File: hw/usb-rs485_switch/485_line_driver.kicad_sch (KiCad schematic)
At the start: 26 parts, among them Q1 MMBT5551, Q2 Si2301CDS, U12 INA180A1, U13 MAX485E

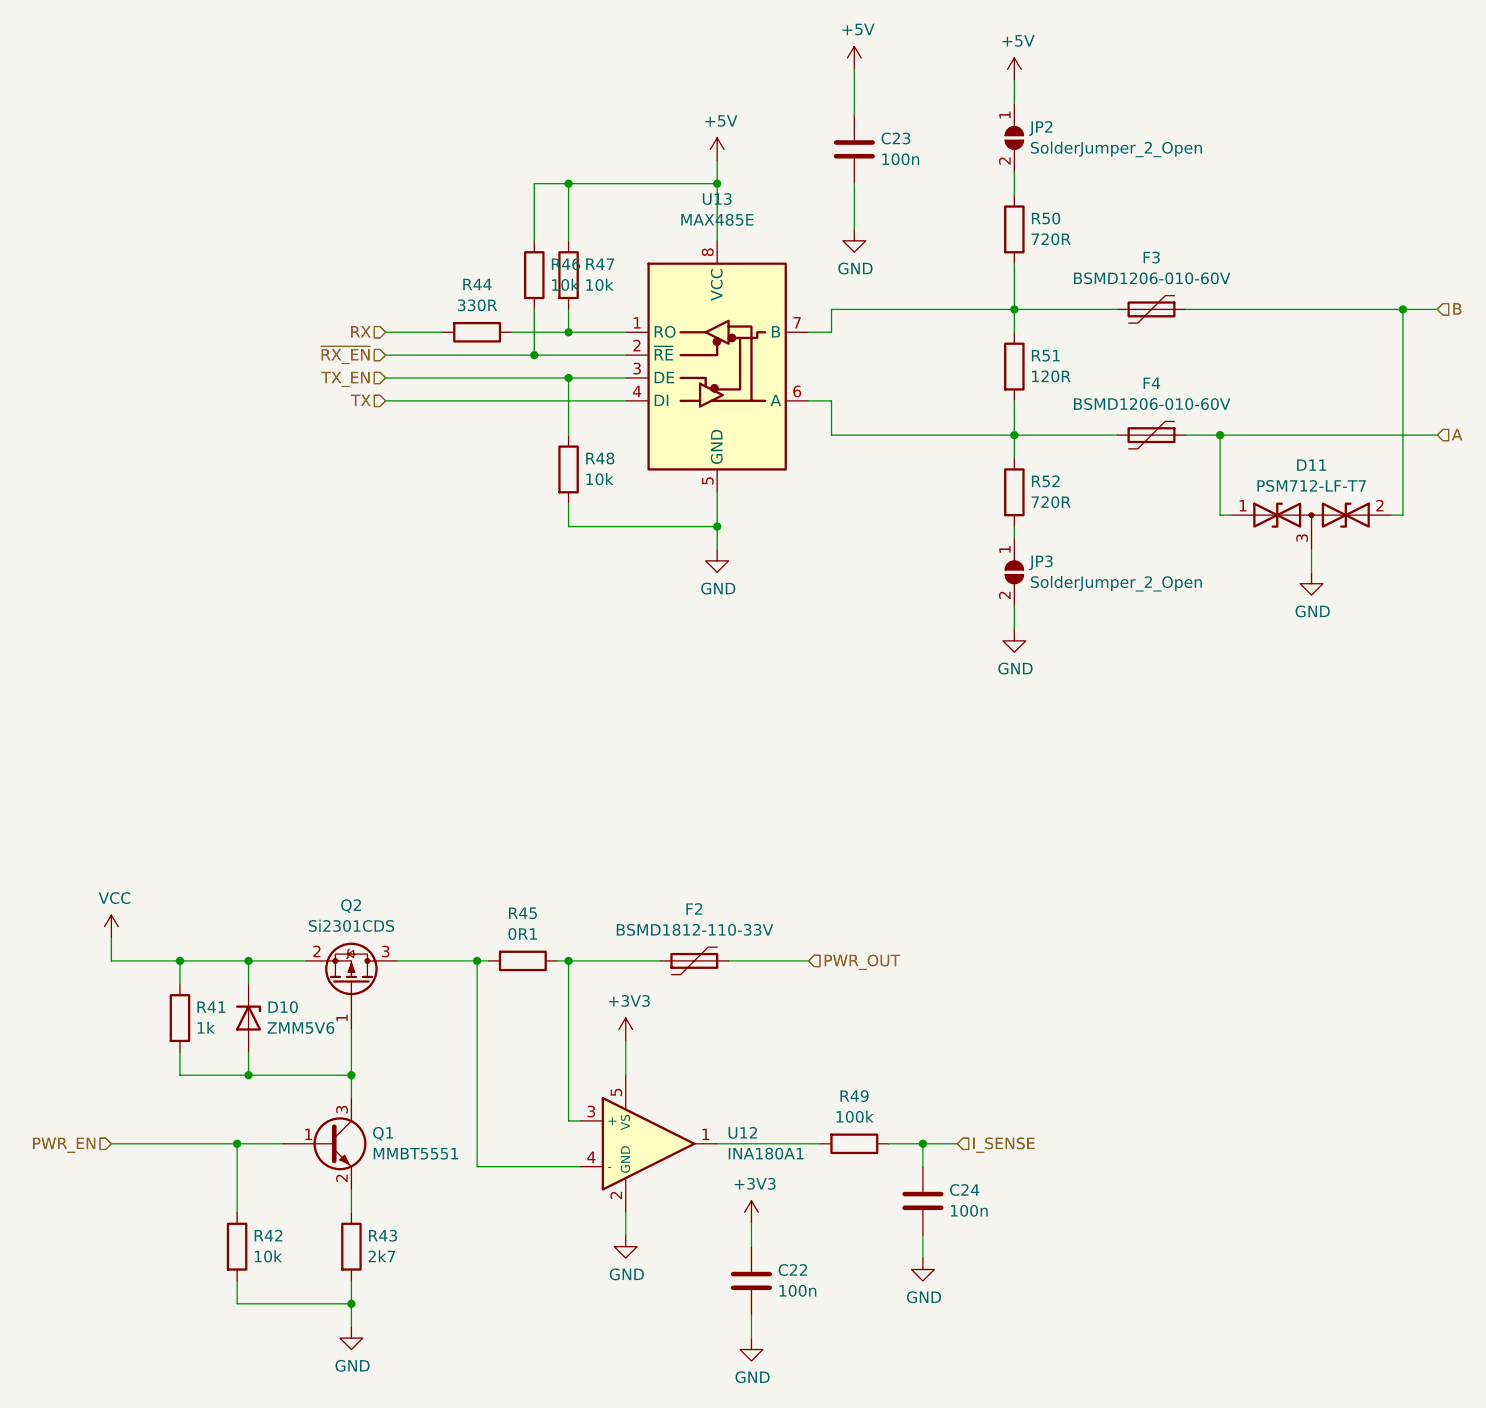
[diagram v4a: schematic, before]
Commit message: Removed unused DCDC, board labels.
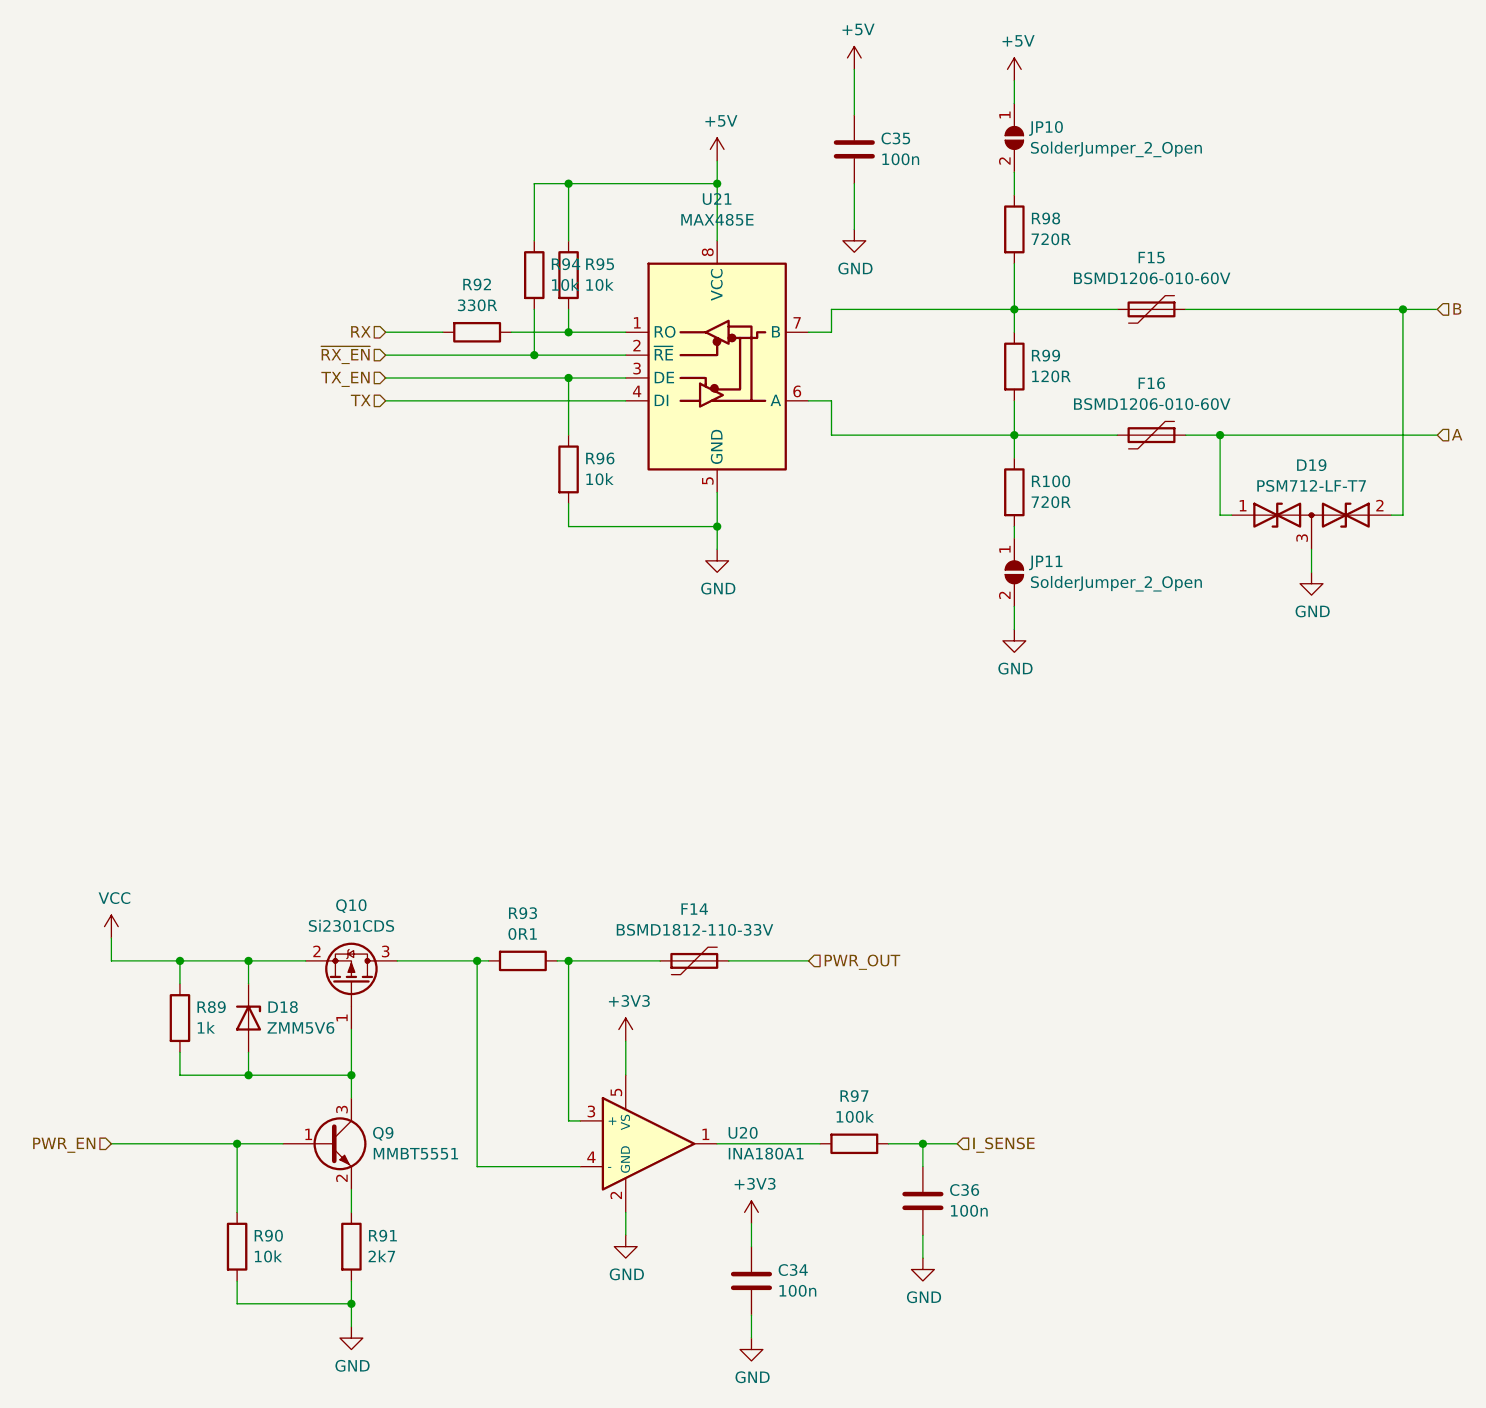
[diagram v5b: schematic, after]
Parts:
- renumbered C22 to C34, C23 to C35, C24 to C36, D10 to D18, D11 to D19, F2 to F14, F3 to F15, F4 to F16, JP2 to JP10, JP3 to JP11, Q2 to Q10, Q1 to Q9, R52 to R100, R41 to R89, R42 to R90, R43 to R91, R44 to R92, R45 to R93, R46 to R94, R47 to R95, R48 to R96, R49 to R97, R50 to R98, R51 to R99, U12 to U20, U13 to U21
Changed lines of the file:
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@@
   (symbol (lib_id "Interface_UART:MAX485E") (at 118.11 67.31 0)
     (in_bom yes) (on_board yes)
-    (property "Reference" "U13" (id 0) (at 118.11 50.0126 0))
+    (property "Reference" "U21" (id 0) (at 118.11 50.0126 0))
     (property "Value" "MAX485E" (id 1) (at 118.11 52.324 0))
     (property "Footprint" "Package_SO:SOIC-8_3.9x4.9mm_P1.27mm" (id 2) (at 118.11 85.09 0)
@@
   (symbol (lib_id "Device:R") (at 151.13 53.34 0)
     (in_bom yes) (on_board yes)
-    (property "Reference" "R50" (id 0) (at 152.908 52.1716 0)
+    (property "Reference" "R98" (id 0) (at 152.908 52.1716 0)
       (effects (font (size 1.27 1.27)) (justify left))
     )
@@
   (symbol (lib_id "Device:R") (at 151.13 68.58 0)
     (in_bom yes) (on_board yes)
-    (property "Reference" "R51" (id 0) (at 152.908 67.4116 0)
+    (property "Reference" "R99" (id 0) (at 152.908 67.4116 0)
       (effects (font (size 1.27 1.27)) (justify left))
     )
@@
   (symbol (lib_id "Device:R") (at 151.13 82.55 0)
     (in_bom yes) (on_board yes)
-    (property "Reference" "R52" (id 0) (at 152.908 81.3816 0)
+    (property "Reference" "R100" (id 0) (at 152.908 81.3816 0)
       (effects (font (size 1.27 1.27)) (justify left))
     )
@@
   (symbol (lib_id "Device:Polyfuse") (at 166.37 62.23 270)
     (in_bom yes) (on_board yes)
-    (property "Reference" "F3" (id 0) (at 166.37 56.515 90))
+    (property "Reference" "F15" (id 0) (at 166.37 56.515 90))
     (property "Value" "BSMD1206-010-60V" (id 1) (at 166.37 58.8264 90))
     (property "Footprint" "Fuse:Fuse_1206_3216Metric" (id 2) (at 161.29 63.5 0)
@@
   (symbol (lib_id "Device:Polyfuse") (at 166.37 76.2 270)
     (in_bom yes) (on_board yes)
-    (property "Reference" "F4" (id 0) (at 166.37 70.485 90))
+    (property "Reference" "F16" (id 0) (at 166.37 70.485 90))
     (property "Value" "BSMD1206-010-60V" (id 1) (at 166.37 72.7964 90))
     (property "Footprint" "Fuse:Fuse_1206_3216Metric" (id 2) (at 161.29 77.47 0)
@@
   (symbol (lib_id "Device:C") (at 133.35 44.45 0)
     (in_bom yes) (on_board yes)
-    (property "Reference" "C23" (id 0) (at 136.271 43.2816 0)
+    (property "Reference" "C35" (id 0) (at 136.271 43.2816 0)
       (effects (font (size 1.27 1.27)) (justify left))
     )
@@
   (symbol (lib_id "Device:R") (at 101.6 58.42 0)
     (in_bom yes) (on_board yes)
-    (property "Reference" "R47" (id 0) (at 103.378 57.2516 0)
+    (property "Reference" "R95" (id 0) (at 103.378 57.2516 0)
       (effects (font (size 1.27 1.27)) (justify left))
     )
@@
   (symbol (lib_id "Device:R") (at 91.44 64.77 270)
     (in_bom yes) (on_board yes)
-    (property "Reference" "R44" (id 0) (at 91.44 59.5122 90))
+    (property "Reference" "R92" (id 0) (at 91.44 59.5122 90))
     (property "Value" "330R" (id 1) (at 91.44 61.8236 90))
     (property "Footprint" "Resistor_SMD:R_0603_1608Metric" (id 2) (at 91.44 62.992 90)
@@
   (symbol (lib_id "Device:D_TVS_x2_AAC") (at 184.15 85.09 0)
     (in_bom yes) (on_board yes)
-    (property "Reference" "D11" (id 0) (at 184.15 79.5782 0))
+    (property "Reference" "D19" (id 0) (at 184.15 79.5782 0))
     (property "Value" "PSM712-LF-T7" (id 1) (at 184.15 81.8896 0))
     (property "Footprint" "Package_TO_SOT_SMD:SOT-23" (id 2) (at 180.34 85.09 0)
@@
   (symbol (lib_id "Arm_interface_board-cache:custom_INA180") (at 110.49 154.94 0)
     (in_bom yes) (on_board yes)
-    (property "Reference" "U12" (id 0) (at 119.2276 153.7716 0)
+    (property "Reference" "U20" (id 0) (at 119.2276 153.7716 0)
       (effects (font (size 1.27 1.27)) (justify left))
     )
@@
   (symbol (lib_id "Device:R") (at 96.52 134.62 270)
     (in_bom yes) (on_board yes)
-    (property "Reference" "R45" (id 0) (at 96.52 129.3622 90))
+    (property "Reference" "R93" (id 0) (at 96.52 129.3622 90))
     (property "Value" "0R1" (id 1) (at 96.52 131.6736 90))
     (property "Footprint" "Resistor_SMD:R_1206_3216Metric" (id 2) (at 96.52 132.842 90)
@@
   (symbol (lib_id "Device:Polyfuse") (at 115.57 134.62 90)
     (in_bom yes) (on_board yes)
-    (property "Reference" "F2" (id 0) (at 115.57 128.905 90))
+    (property "Reference" "F14" (id 0) (at 115.57 128.905 90))
     (property "Value" "BSMD1812-110-33V" (id 1) (at 115.57 131.2164 90))
     (property "Footprint" "Fuse:Fuse_1812_4532Metric" (id 2) (at 120.65 133.35 0)
@@
   (symbol (lib_id "Transistor_FET:Si2319CDS") (at 77.47 137.16 270) (mirror x)
     (in_bom yes) (on_board yes)
-    (property "Reference" "Q2" (id 0) (at 77.47 128.4732 90))
+    (property "Reference" "Q10" (id 0) (at 77.47 128.4732 90))
     (property "Value" "Si2301CDS" (id 1) (at 77.47 130.7846 90))
     (property "Footprint" "Package_TO_SOT_SMD:SOT-23" (id 2) (at 75.565 132.08 0)
@@
   (symbol (lib_id "Device:R") (at 58.42 140.97 0)
     (in_bom yes) (on_board yes)
-    (property "Reference" "R41" (id 0) (at 60.198 139.8016 0)
+    (property "Reference" "R89" (id 0) (at 60.198 139.8016 0)
       (effects (font (size 1.27 1.27)) (justify left))
     )
@@
   (symbol (lib_id "Diode:ZMMxx") (at 66.04 140.97 270)
     (in_bom yes) (on_board yes)
-    (property "Reference" "D10" (id 0) (at 68.072 139.8016 90)
+    (property "Reference" "D18" (id 0) (at 68.072 139.8016 90)
       (effects (font (size 1.27 1.27)) (justify left))
     )
@@
   (symbol (lib_id "Device:Q_NPN_BEC") (at 74.93 154.94 0)
     (in_bom yes) (on_board yes)
-    (property "Reference" "Q1" (id 0) (at 79.7814 153.7716 0)
+    (property "Reference" "Q9" (id 0) (at 79.7814 153.7716 0)
       (effects (font (size 1.27 1.27)) (justify left))
     )
@@
   (symbol (lib_id "Device:R") (at 77.47 166.37 0)
     (in_bom yes) (on_board yes)
-    (property "Reference" "R43" (id 0) (at 79.248 165.2016 0)
+    (property "Reference" "R91" (id 0) (at 79.248 165.2016 0)
       (effects (font (size 1.27 1.27)) (justify left))
     )
@@
   (symbol (lib_id "Device:C") (at 121.92 170.18 0)
     (in_bom yes) (on_board yes)
-    (property "Reference" "C22" (id 0) (at 124.841 169.0116 0)
+    (property "Reference" "C34" (id 0) (at 124.841 169.0116 0)
       (effects (font (size 1.27 1.27)) (justify left))
     )
@@
   (symbol (lib_id "Device:R") (at 97.79 58.42 0)
     (in_bom yes) (on_board yes)
-    (property "Reference" "R46" (id 0) (at 99.568 57.2516 0)
+    (property "Reference" "R94" (id 0) (at 99.568 57.2516 0)
       (effects (font (size 1.27 1.27)) (justify left))
     )
@@
   (symbol (lib_id "Device:R") (at 101.6 80.01 0)
     (in_bom yes) (on_board yes)
-    (property "Reference" "R48" (id 0) (at 103.378 78.8416 0)
+    (property "Reference" "R96" (id 0) (at 103.378 78.8416 0)
       (effects (font (size 1.27 1.27)) (justify left))
     )
@@
   (symbol (lib_id "Device:R") (at 64.77 166.37 0)
     (in_bom yes) (on_board yes)
-    (property "Reference" "R42" (id 0) (at 66.548 165.2016 0)
+    (property "Reference" "R90" (id 0) (at 66.548 165.2016 0)
       (effects (font (size 1.27 1.27)) (justify left))
     )
@@
   (symbol (lib_id "Jumper:SolderJumper_2_Open") (at 151.13 91.44 270)
     (in_bom yes) (on_board yes)
-    (property "Reference" "JP3" (id 0) (at 152.8572 90.2716 90)
+    (property "Reference" "JP11" (id 0) (at 152.8572 90.2716 90)
       (effects (font (size 1.27 1.27)) (justify left))
     )
@@
   (symbol (lib_id "Jumper:SolderJumper_2_Open") (at 151.13 43.18 270)
     (in_bom yes) (on_board yes)
-    (property "Reference" "JP2" (id 0) (at 152.8572 42.0116 90)
+    (property "Reference" "JP10" (id 0) (at 152.8572 42.0116 90)
       (effects (font (size 1.27 1.27)) (justify left))
     )
@@
   (symbol (lib_id "Device:R") (at 133.35 154.94 270)
     (in_bom yes) (on_board yes)
-    (property "Reference" "R49" (id 0) (at 133.35 149.6822 90))
+    (property "Reference" "R97" (id 0) (at 133.35 149.6822 90))
     (property "Value" "100k" (id 1) (at 133.35 151.9936 90))
     (property "Footprint" "Resistor_SMD:R_0603_1608Metric" (id 2) (at 133.35 153.162 90)
@@
   (symbol (lib_id "Device:C") (at 140.97 161.29 0)
     (in_bom yes) (on_board yes)
-    (property "Reference" "C24" (id 0) (at 143.891 160.1216 0)
-      (effects (font (size 1.27 1.27)) (justify left))
-    )
+    (property "Reference" "C36" (id 0) (at 143.891 160.1216 0)
+      (effects (font (size 1.27 1.27)) (justify left))
+    )

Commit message: Final changes.
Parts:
- C43: renamed from C34; LCSC (none) -> C14663
- C44: renamed from C35; LCSC (none) -> C14663
- C45: renamed from C36; LCSC (none) -> C14663
- R125: renamed from R89; LCSC (none) -> C21190
- R126: renamed from R90; LCSC (none) -> C25804
- R127: renamed from R91; LCSC (none) -> C13167
- R128: renamed from R92; LCSC (none) -> C23138
- R130: renamed from R94; LCSC (none) -> C25804
- R131: renamed from R95; LCSC (none) -> C25804
- R132: renamed from R96; LCSC (none) -> C25804
- R133: renamed from R97; LCSC (none) -> C25803
- R134: renamed from R98; LCSC (none) -> C23241
- R135: renamed from R99; LCSC (none) -> C22787
- R136: renamed from R100; LCSC (none) -> C23241
- renumbered D18 to D24, D19 to D25, F14 to F23, F15 to F24, F16 to F25, JP10 to JP16, JP11 to JP17, Q9 to Q15, Q10 to Q16, R93 to R129, U20 to U26, U21 to U27
